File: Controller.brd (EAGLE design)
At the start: 160 x 100 mm, 52 parts, among them SW1 MULTICOLOR_BUTTON, SW2 MULTICOLOR_BUTTON, SW3 MULTICOLOR_BUTTON, SW4 MULTICOLOR_BUTTON, SW5 MULTICOLOR_BUTTON, SW6 MULTICOLOR_BUTTON, SW7 MULTICOLOR_BUTTON, SW8 MULTICOLOR_BUTTON, U1 ATMEGA328-PU, U2 MCP6002T-I/SNSOIC8-N_MC-M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

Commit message: Fixed connection error in Low Pass filter
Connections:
- removed net N$13: U2.6, U2.7
- removed net N$2: U2.1, U2.2
- net LEFT_BUTTON_OUTPUT: now also U2.3
- net LEFT_OUTPUT: now also U2.1, U2.2; no longer U2.3
- net RIGHT_BUTTON_OUTPUT: now also U2.5
- net RIGHT_OUTPUT: now also U2.6, U2.7; no longer U2.5
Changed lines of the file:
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@@
 <contactref element="S2" pad="B2A"/>
 <contactref element="R2" pad="2"/>
-<contactref element="U2" pad="5"/>
-<wire x1="-39.497" y1="95.885" x2="-30.01" y2="85.17" width="0" layer="19" extent="1-1"/>
-<wire x1="-45.25" y1="85.17" x2="-39.497" y2="95.885" width="0" layer="19" extent="1-1"/>
+<contactref element="U2" pad="6"/>
+<contactref element="U2" pad="7"/>
+<wire x1="-39.497" y1="98.425" x2="-39.497" y2="97.155" width="0" layer="19" extent="1-1"/>
+<wire x1="-45.25" y1="85.17" x2="-39.497" y2="97.155" width="0" layer="19" extent="1-1"/>
+<wire x1="-30.01" y1="85.17" x2="-45.25" y2="85.17" width="0" layer="19" extent="1-1"/>
 <wire x1="-60.49" y1="85.17" x2="-45.25" y2="85.17" width="0" layer="19" extent="1-1"/>
 <wire x1="-75.73" y1="85.17" x2="-60.49" y2="85.17" width="0" layer="19" extent="1-1"/>
@@
 <contactref element="S1" pad="B2A"/>
 <contactref element="R1" pad="2"/>
-<contactref element="U2" pad="3"/>
+<contactref element="U2" pad="2"/>
+<contactref element="U2" pad="1"/>
 <wire x1="-38.9" y1="66.12" x2="-14.77" y2="85.17" width="0" layer="19" extent="1-1"/>
 <wire x1="-29.92" y1="55.28" x2="-38.9" y2="66.12" width="0" layer="19" extent="1-1"/>
 <wire x1="-54.14" y1="66.12" x2="-38.9" y2="66.12" width="0" layer="19" extent="1-1"/>
 <wire x1="-69.38" y1="66.12" x2="-54.14" y2="66.12" width="0" layer="19" extent="1-1"/>
-<wire x1="-44.323" y1="97.155" x2="-38.9" y2="66.12" width="0" layer="19" extent="1-1"/>
-<wire x1="-67.158" y1="97.79" x2="-44.323" y2="97.155" width="0" layer="19" extent="1-1"/>
+<wire x1="-67.158" y1="97.79" x2="-69.38" y2="66.12" width="0" layer="19" extent="1-1"/>
+<wire x1="-44.323" y1="98.425" x2="-67.158" y2="97.79" width="0" layer="19" extent="1-1"/>
+<wire x1="-44.323" y1="99.695" x2="-44.323" y2="98.425" width="0" layer="19" extent="1-1"/>
 <wire x1="-13.97" y1="21.59" x2="-29.92" y2="55.28" width="0" layer="19" extent="1-1"/>
 <wire x1="-13.97" y1="1.27" x2="-13.97" y2="21.59" width="0" layer="19" extent="1-1"/>
@@
 <contactref element="C1" pad="1"/>
 <contactref element="R1" pad="1"/>
+<contactref element="U2" pad="3"/>
+<wire x1="-50.93" y1="97.79" x2="-44.323" y2="97.155" width="0" layer="19" extent="1-1"/>
 <wire x1="-70.002" y1="97.79" x2="-50.93" y2="97.79" width="0" layer="19" extent="1-1"/>
 </signal>
@@
 <contactref element="C2" pad="1"/>
 <contactref element="R2" pad="1"/>
+<contactref element="U2" pad="5"/>
+<wire x1="-57.28" y1="97.79" x2="-39.497" y2="95.885" width="0" layer="19" extent="1-1"/>
 <wire x1="-76.352" y1="97.79" x2="-57.28" y2="97.79" width="0" layer="19" extent="1-1"/>
 </signal>
-<signal name="N$2">
-<contactref element="U2" pad="2"/>
-<contactref element="U2" pad="1"/>
-<wire x1="-44.323" y1="98.425" x2="-44.323" y2="99.695" width="0" layer="19" extent="1-1"/>
-</signal>
-<signal name="N$13">
-<contactref element="U2" pad="6"/>
-<contactref element="U2" pad="7"/>
-<wire x1="-39.497" y1="98.425" x2="-39.497" y2="97.155" width="0" layer="19" extent="1-1"/>
-</signal>
 <signal name="5V">

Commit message: Added more holes, did some routing added 3D models
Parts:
- removed C5: (no value), eagle-ltspice:C1206
- removed R31, R32, R33, R34, R35: (no value), resistor:M1206
- removed S3, S4: (no value), SparkFun-Switches:SWITCH_SPDT_PTH_11.6X4.0MM
- removed U$2, U$3: BUMPER, Bumper:BUMPER
- removed U$4: SWITCH, 3 Pole Double Throw Switch:SWITCH
- moved C6 207.8 mm to (57.0, 44.1), turned to 180 degrees
- moved C4 198.3 mm to (57.0, 29.3), turned to 180 degrees
- moved R13 198.1 mm to (117.6, 6.10), turned to 90 degrees
- moved R14 196.9 mm to (111.2, 6.38), turned to 270 degrees
- moved SW7 194.7 mm to (117.0, 45.0)
- moved Y1 194.4 mm to (57.1, 36.9), flipped to the bottom, turned to 90 degrees
- moved R12 190.6 mm to (117.6, 12.3), turned to 90 degrees
- moved SW8 186.2 mm to (93.0, 45.0)
- moved R11 183.0 mm to (117.6, 18.7), turned to 90 degrees
- moved R2 175.9 mm to (89.7, 35.9)
- moved R10 175.1 mm to (117.5, 25.4), turned to 90 degrees
- moved SW6 171.9 mm to (105.0, 33.0)
- moved XB2 171.2 mm to (62.5, 36.2), turned to 180 degrees
- moved R9 167.5 mm to (117.5, 32.1), turned to 90 degrees
- moved SW5 150.6 mm to (105.0, 57.0)
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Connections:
- removed net 5V: R31.2, U$2.P$1
- removed net BUT_OUT_BUMP: C5.1, R35.2, S3.3, S4.3, U$2.P$2, U$3.P$2
- removed net N$19: R31.1, R32.2, U$3.P$1
- removed net N$20: R32.1, R33.2, S3.2
- removed net N$21: R33.1, R34.2, S4.2
- net GND: no longer C5.2, R34.1, R35.1, U$2.P$3, U$2.P$4, U$3.P$3, U$3.P$4
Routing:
- net LEFT_OUTPUT: track 0.00 -> 98.3 mm
- net RIGHT_OUTPUT: track 0.00 -> 92.5 mm
- net N$8: track 0.00 -> 61.7 mm
- net N$9: track 0.00 -> 50.0 mm
- net N$6: track 0.00 -> 38.2 mm, vias 0 -> 2
- net N$5: track 0.00 -> 30.5 mm
- net N$7: track 0.00 -> 27.9 mm, vias 0 -> 2
- net N$12: track 0.00 -> 6.70 mm
- net N$4: track 0.00 -> 4.04 mm
- net N$3: track 0.00 -> 3.84 mm
- net N$10: track 0.00 -> 3.54 mm
- net N$11: track 0.00 -> 3.34 mm
- added copper zone on layer 1, net GND
- added copper zone on layer 16, net GND
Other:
- board size 160 x 100 mm -> 125 x 65 mm

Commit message: MORE ROUTING!!
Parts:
- moved C2 162.0 mm to (92.3, 32.3)
- moved C3 154.3 mm to (67.6, 14.3), turned to 270 degrees
- moved C1 109.2 mm to (38.7, 33.4), turned to 180 degrees
- moved U2 5.11 mm to (62.2, 14.9)
- moved S5 4.50 mm to (62.5, 6.56)
- moved R1 4.17 mm to (38.6, 37.0), turned to 180 degrees
- moved R2 2.79 mm to (92.4, 35.2)
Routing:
- net RIGHT_OUTPUT: track 92.5 -> 133.7 mm, vias 0 -> 2
- net N$10: track 3.54 -> 39.8 mm, vias 0 -> 1
- net LEFT_BUTTON_OUTPUT: track 0.00 -> 33.8 mm
- net LEFT_OUTPUT: track 98.3 -> 120.8 mm, vias 0 -> 1
- net +5V: track 0.00 -> 17.6 mm
- net RIGHT_BUTTON_OUTPUT: track 0.00 -> 7.59 mm

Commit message: Routing
Routed most of the board. Need to add power components and Zeners
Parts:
- moved R15 196.7 mm to (76.8, 31.0), turned to 90 degrees
- moved U$1 183.7 mm to (41.2, 42.5)
- moved R17 183.1 mm to (47.0, 47.7), turned to 270 degrees
- moved R19 182.7 mm to (41.3, 47.7), turned to 270 degrees
- moved U$5 178.8 mm to (47.0, 42.4)
- moved R16 178.5 mm to (47.2, 39.0), turned to 180 degrees
- moved R18 176.5 mm to (40.9, 39.0), turned to 180 degrees
- moved C4 12.1 mm to (56.8, 41.4)
- moved C6 11.5 mm to (56.8, 32.6)
- moved C1 1.80 mm to (38.8, 31.6)
- moved R1 1.80 mm to (38.7, 35.2)
- moved Y1 0.39 mm to (56.7, 37.0), turned to 270 degrees
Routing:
- net +3V3: track 0.00 -> 68.1 mm, vias 0 -> 4
- net +5V: track 17.6 -> 85.6 mm, vias 0 -> 10
- net Y_LEFT: track 0.00 -> 66.2 mm, vias 0 -> 1
- net N$17: track 0.00 -> 54.3 mm, vias 0 -> 1
- net X_RIGHT: track 0.00 -> 53.7 mm, vias 0 -> 2
- net N$14: track 0.00 -> 53.5 mm, vias 0 -> 1
- net X_LEFT: track 0.00 -> 53.3 mm, vias 0 -> 2
- net N$11: track 3.34 -> 56.4 mm, vias 0 -> 1
- net GND: track 0.00 -> 51.2 mm, vias 24 -> 33
- net Y_RIGHT: track 0.00 -> 49.6 mm, vias 0 -> 2
- net N$3: track 3.84 -> 43.0 mm, vias 0 -> 2
- net LEFT_OUTPUT: track 120.8 -> 159.9 mm
- net RIGHT_OUTPUT: track 133.7 -> 170.4 mm
- net RIGHT_BUTTON_OUTPUT: track 7.59 -> 42.1 mm
- net RX: track 0.00 -> 28.6 mm
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- added copper zone on layer 1, net +5V

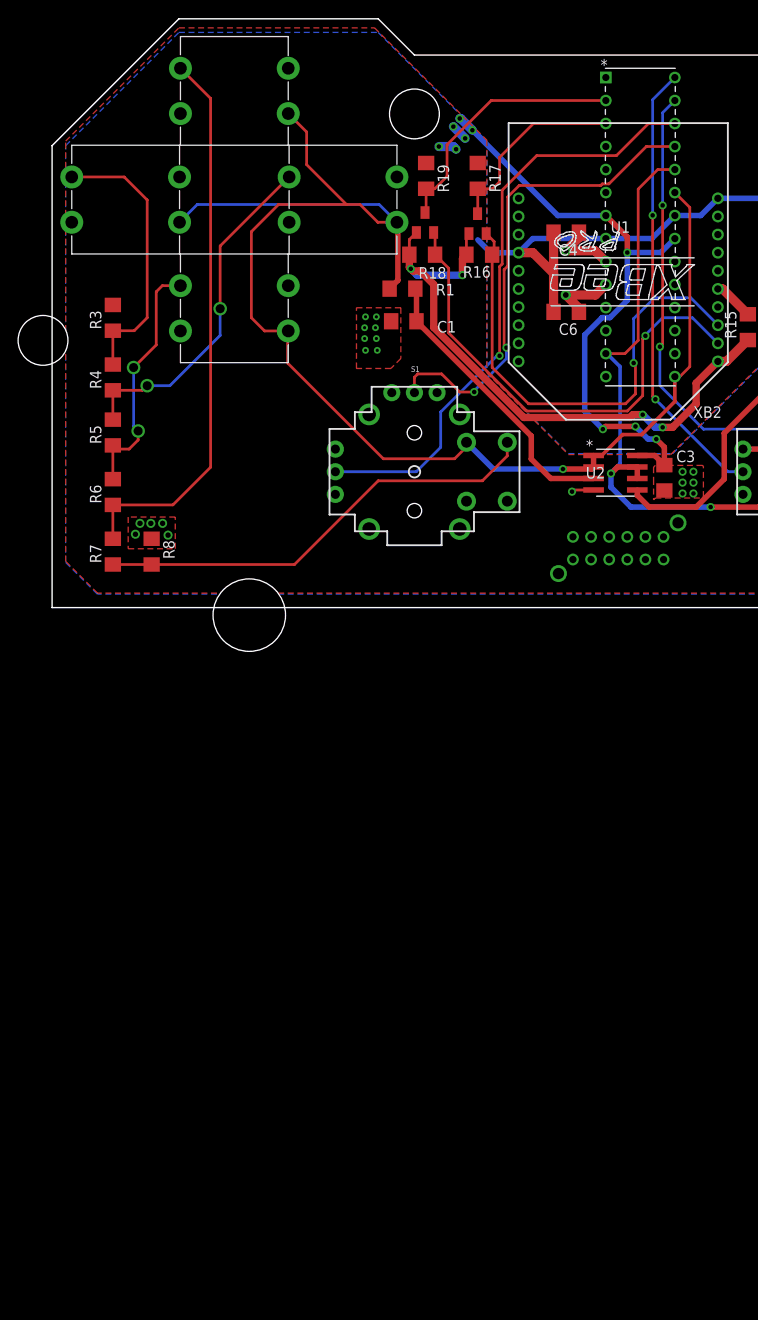
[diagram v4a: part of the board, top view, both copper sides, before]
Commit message: Changes
Added more 3D models. Changed to a ATMega2560
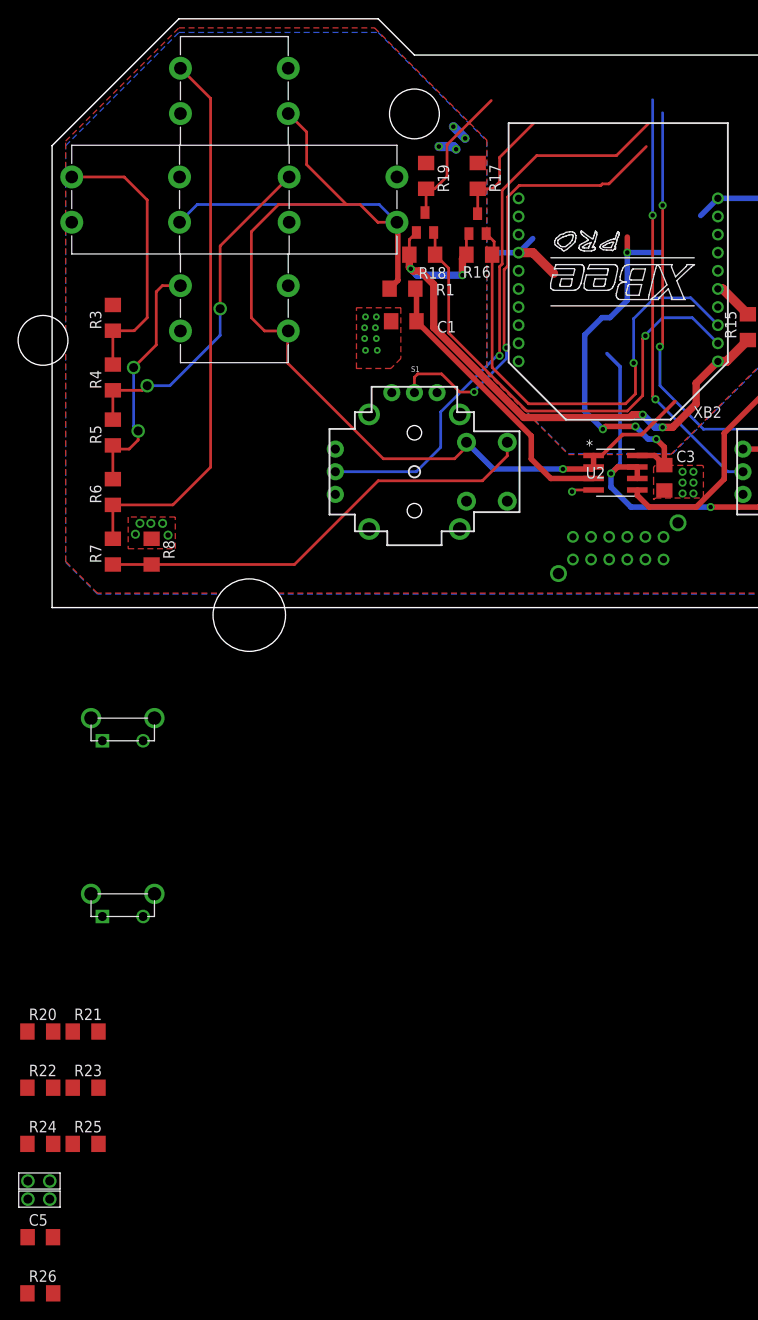
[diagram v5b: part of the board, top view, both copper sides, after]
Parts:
- removed C4, C6: 22pF, rcl:C1206
- removed U1: ATMEGA328-PU, Controller:28P3
- removed Y1: ECS-160-20-4X, ECS-160-20-4X:XTAL_ECS-160-20-4X
- added C5: 22pF, rcl:C1206
- added R20, R21, R22, R23: 1k, rcl:R1206
- added R24, R25: 10k, rcl:R1206
- added R26: 100k, rcl:R1206
- added SW10, SW9: MY_LBR_SPSTSWITCH, Controller:MY_LBR_2HOLES
- added U$2, U$3: BUMPER_BUMPER, Controller:BUMPER_BUMPER
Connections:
- removed net AVCC: U1.20
- removed net N$15: C6.1, U1.10, Y1.2
- removed net N$16: C4.1, U1.9, Y1.1
- new net N$13: R21.1, R22.2, U$3.P$1
- new net N$18: R22.1, R23.2, SW9.P$1
- new net N$19: R23.1, R24.2, SW10.P$1
- new net N$2: R20.1, R21.2, U$2.P$1
- new net N$20: R24.1, R25.2
- new net N$21: R26.2, SW10.P$2, SW9.P$2, U$2.P$2, U$3.P$2
- net +5V: now also R20.2; no longer U1.21, U1.7
- net GND: now also C5.2, R25.1, U$2.P$3, U$2.P$4, U$3.P$3, U$3.P$4; no longer C4.2, C6.2, U1.22, U1.8
- net LEFT_BUTTON_OUTPUT: now also C5.1, R26.1
- net LEFT_OUTPUT: no longer U1.15, U1.23
- net RIGHT_OUTPUT: no longer U1.13, U1.24
- net RX: no longer U1.2
- net TX: no longer U1.3
- net X_LEFT: no longer U1.25
- net X_RIGHT: no longer U1.27
- net Y_LEFT: no longer U1.26
- net Y_RIGHT: no longer U1.28
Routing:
- net GND: track 51.2 -> 20.8 mm
- net +5V: track 85.6 -> 59.5 mm, vias 10 -> 8
- net RIGHT_OUTPUT: track 170.4 -> 144.4 mm
- net LEFT_OUTPUT: track 159.9 -> 135.1 mm
- net RX: track 28.6 -> 16.0 mm
- net TX: track 21.5 -> 13.5 mm
- net N$16: track 7.52 -> 0.00 mm
- net N$15: track 7.36 -> 0.00 mm
- net Y_RIGHT: track 49.6 -> 46.2 mm
- net X_LEFT: track 53.3 -> 50.2 mm
- net Y_LEFT: track 66.2 -> 63.3 mm
- net X_RIGHT: track 53.7 -> 51.8 mm

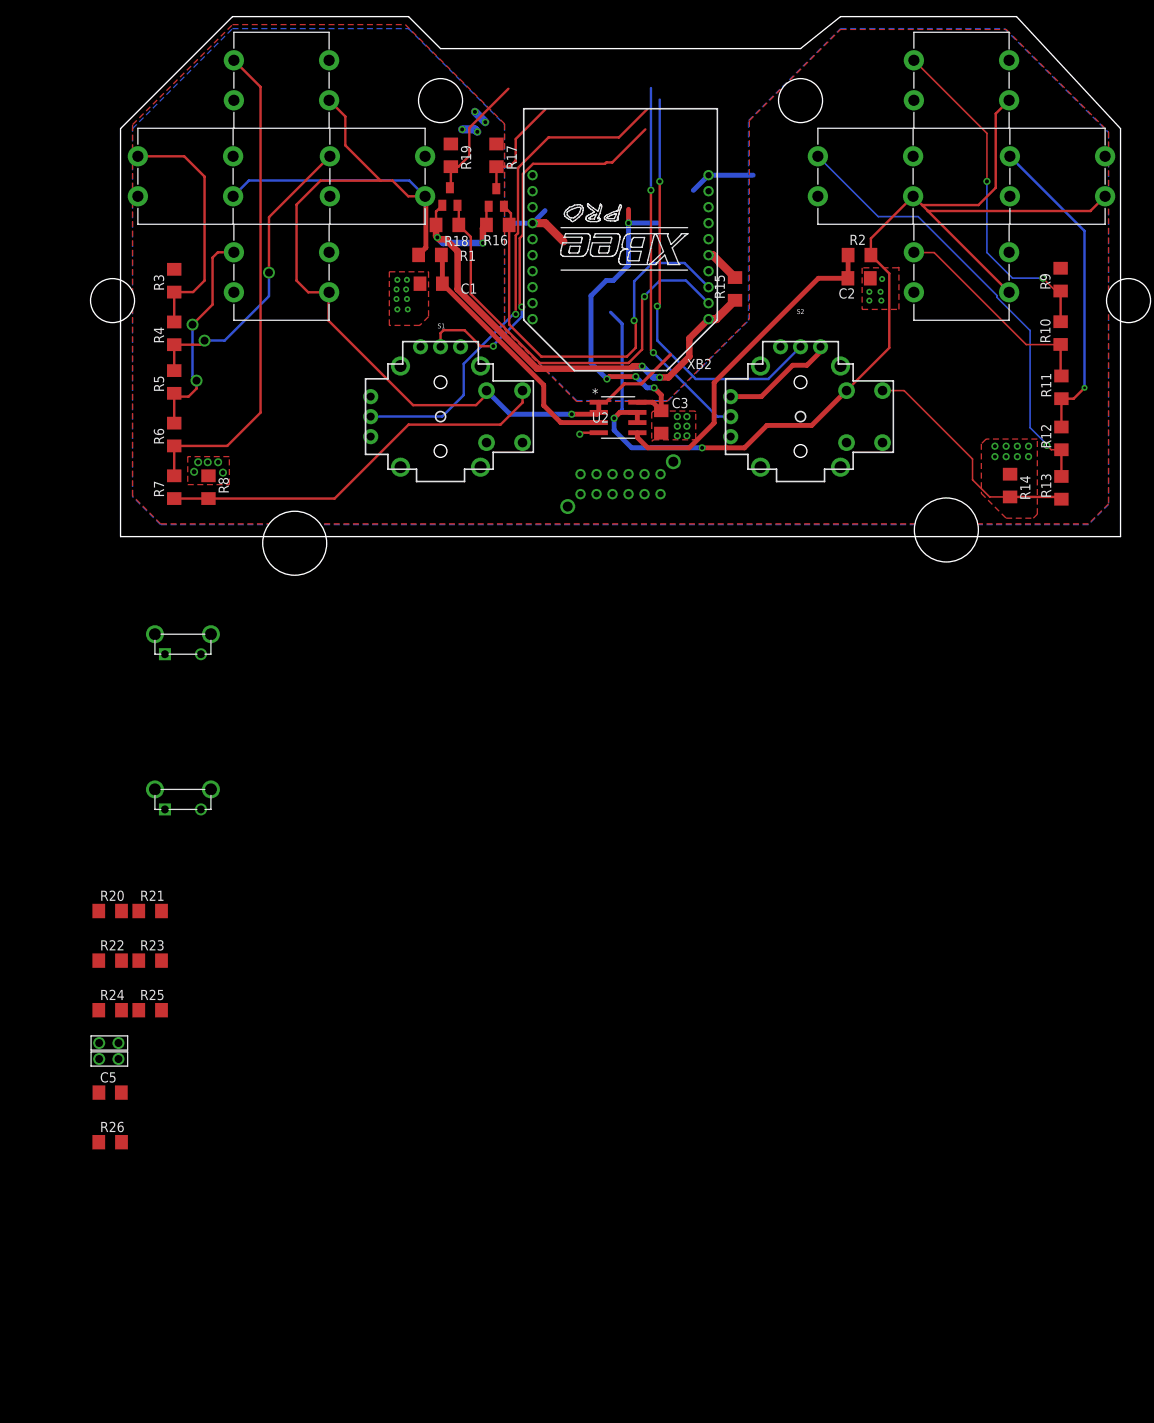
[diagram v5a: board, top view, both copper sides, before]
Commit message: Added Charlieplexed button matrix
Will now have to turn on PORTB bits 1:3
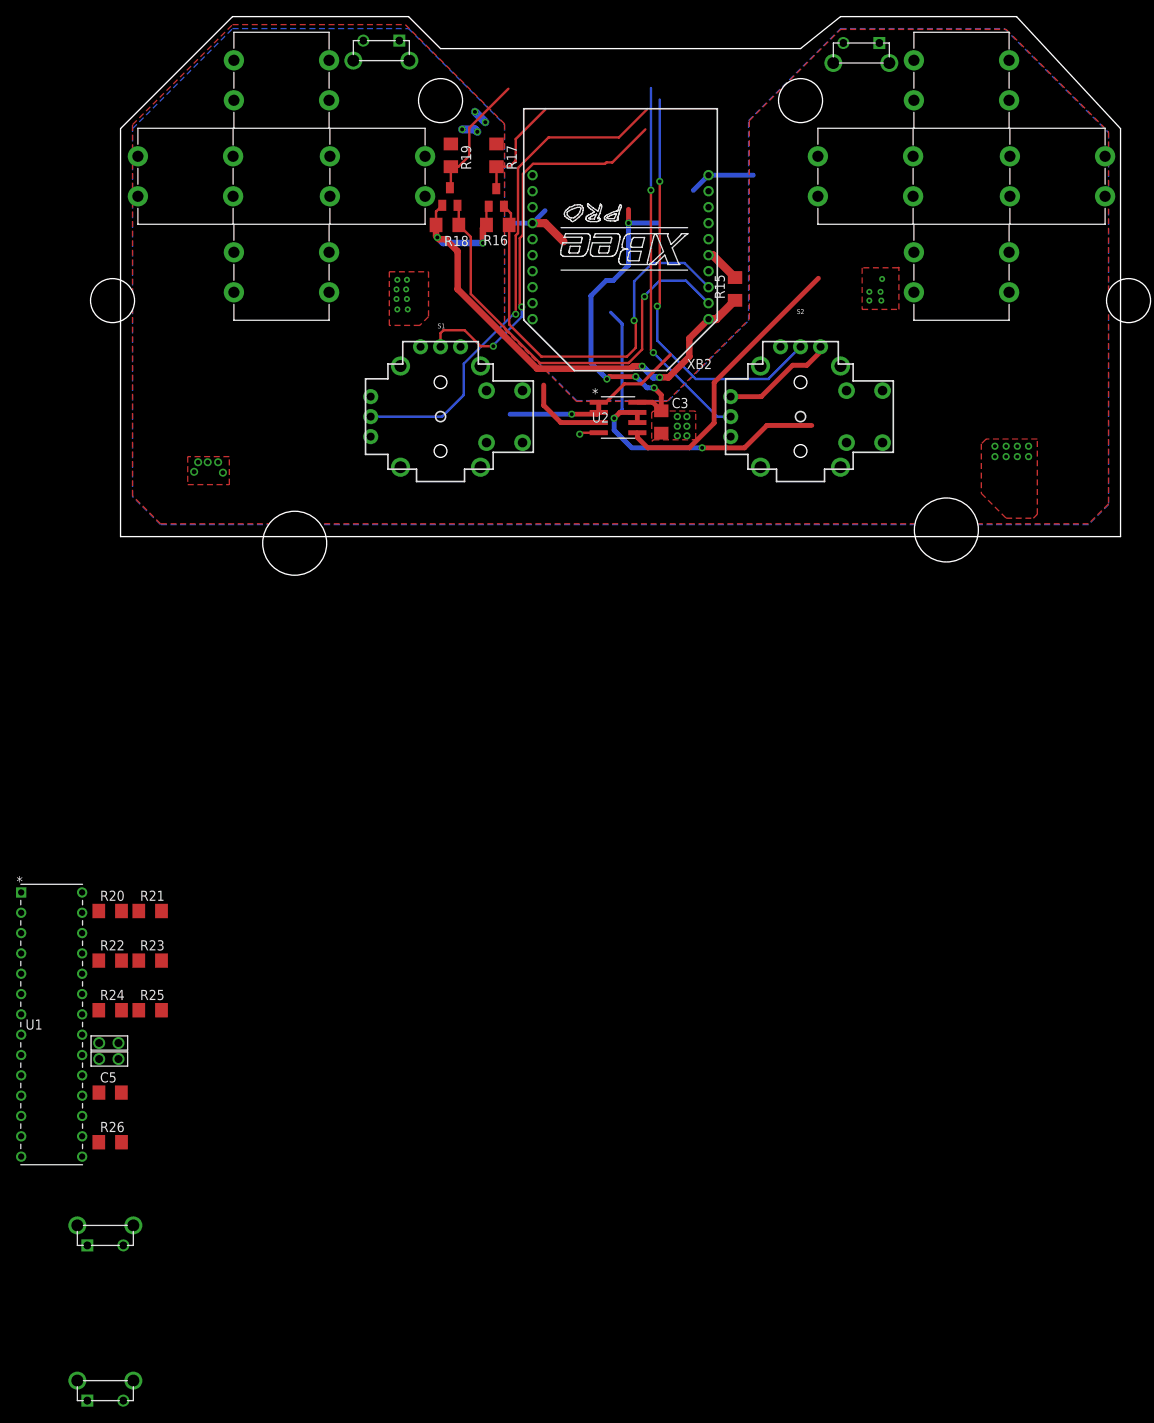
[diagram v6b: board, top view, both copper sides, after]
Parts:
- removed C1, C2: 22pF, rcl:C1206
- removed R1, R2: 100k, rcl:R1206
- removed R10, R11, R12, R3, R4, R5, R6, R9: 1k, rcl:R1206
- removed R13, R14, R7, R8: 10k, rcl:R1206
- removed S5: EG4208A, SamacSys_Parts:EG4208A
- added U$4, U$6: BUMPER_BUMPER, Controller:BUMPER_BUMPER
- added U1: ATMEGA328-PU, Controller:28P3
- moved U$3 127.9 mm to (92.6, 61.7), turned to 180 degrees
- moved U$2 80.6 mm to (32.6, 62.0), turned to 180 degrees
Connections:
- removed net N$10: R11.1, R12.2, SW7.2
- removed net N$11: R12.1, R13.2, SW8.2
- removed net N$12: R13.1, R14.2, S2.B1A
- removed net N$6: R4.1, R5.2, SW2.2
- removed net N$7: R5.1, R6.2, SW3.2
- removed net N$8: R6.1, R7.2, SW4.2
- removed net N$9: R7.1, R8.2, S1.B1A
- new net AREF: U1.21
- new net AVCC: U1.20
- new net C1: S1.B2A, SW1.4, SW5.4
- new net C2: S2.B2A, SW2.4, SW6.4
- new net C3: SW3.4, SW7.4, U$4.P$4
- new net C4: SW4.4, SW8.4, U$6.P$4
- new net N$24: U1.24
- new net N$25: U1.23
- net +5V: now also U1.7; no longer R3.2, R9.2
- net GND: now also U1.22, U1.8; no longer C1.2, C2.2, R14.1, R8.1
- net LEFT_BUTTON_OUTPUT: no longer C1.1, R1.1
- net LEFT_OUTPUT: no longer R1.2, S1.B2A, SW1.4, SW2.4, SW3.4, SW4.4
- net N$3: now also SW1.2, SW2.2, SW3.2, SW4.2; no longer R10.2, R9.1, SW5.2
- net N$4: now also SW5.2, SW7.2, SW8.2; no longer R10.1, R11.2
- net N$5: now also S1.B1A, S2.B1A, U$4.P$1, U$6.P$1; no longer R3.1, R4.2, SW1.2
- net RIGHT_BUTTON_OUTPUT: no longer C2.1, R2.1
- net RIGHT_OUTPUT: no longer R2.2, S2.B2A, SW5.4, SW6.4, SW7.4, SW8.4
- net X_LEFT: now also U1.28
- net X_RIGHT: now also U1.27
- net Y_LEFT: now also U1.26
- net Y_RIGHT: now also U1.25
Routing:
- net LEFT_OUTPUT: track 135.1 -> 23.9 mm
- net RIGHT_OUTPUT: track 144.4 -> 47.0 mm
- net N$8: track 61.7 -> 0.00 mm
- net N$11: track 56.4 -> 0.00 mm, vias 1 -> 0
- net N$9: track 50.0 -> 0.00 mm
- net N$3: track 43.0 -> 0.00 mm, vias 2 -> 0
- net N$10: track 39.8 -> 0.00 mm, vias 1 -> 0
- net N$6: track 38.2 -> 0.00 mm, vias 2 -> 0
- net N$5: track 30.5 -> 0.00 mm
- net N$12: track 29.9 -> 0.00 mm
- net N$7: track 27.9 -> 0.00 mm, vias 2 -> 0
- net N$4: track 27.2 -> 0.00 mm
- net LEFT_BUTTON_OUTPUT: track 32.0 -> 10.3 mm
- net RIGHT_BUTTON_OUTPUT: track 42.1 -> 35.5 mm
